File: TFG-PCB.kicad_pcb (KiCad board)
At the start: 2 copper layers, 38.1 x 38.1 mm, 25 parts, among them J1 TYPE-C-31-M-12, SW1 SW_Push, U1 ATmega32U4-AU, Y1 16MHz

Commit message: Added 60% keyboard schematics and started routing wires
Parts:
- added D10: SOD-123, Diode_SMD:D_SOD-123, B.Cu at (304.0, 165.9)
- added D11: SOD-123, Diode_SMD:D_SOD-123, B.Cu at (323.1, 165.9)
- added D12: SOD-123, Diode_SMD:D_SOD-123, B.Cu at (342.1, 165.9)
- added D13: SOD-123, Diode_SMD:D_SOD-123, B.Cu at (361.2, 165.9)
- added D14: SOD-123, Diode_SMD:D_SOD-123, B.Cu at (389.7, 165.9)
- added D15: SOD-123, Diode_SMD:D_SOD-123, B.Cu at (137.3, 184.9)
- added D16: SOD-123, Diode_SMD:D_SOD-123, B.Cu at (161.1, 184.9)
- added D17: SOD-123, Diode_SMD:D_SOD-123, B.Cu at (180.2, 184.9)
- added D18: SOD-123, Diode_SMD:D_SOD-123, B.Cu at (199.2, 184.9)
- added D19: SOD-123, Diode_SMD:D_SOD-123, B.Cu at (218.3, 184.9)
- added D20: SOD-123, Diode_SMD:D_SOD-123, B.Cu at (237.3, 184.9)
- added D21: SOD-123, Diode_SMD:D_SOD-123, B.Cu at (256.4, 184.9)
- added D22: SOD-123, Diode_SMD:D_SOD-123, B.Cu at (275.4, 184.9)
- added D23: SOD-123, Diode_SMD:D_SOD-123, B.Cu at (294.5, 184.9)
- added D24: SOD-123, Diode_SMD:D_SOD-123, B.Cu at (313.5, 184.9)
- added D25: SOD-123, Diode_SMD:D_SOD-123, B.Cu at (332.6, 184.9)
- added D26: SOD-123, Diode_SMD:D_SOD-123, B.Cu at (351.6, 184.9)
- added D27: SOD-123, Diode_SMD:D_SOD-123, B.Cu at (370.7, 184.9)
- added D28: SOD-123, Diode_SMD:D_SOD-123, B.Cu at (396.9, 194.5)
- added D29: SOD-123, Diode_SMD:D_SOD-123, B.Cu at (139.7, 204.0)
- added D30: SOD-123, Diode_SMD:D_SOD-123, B.Cu at (165.9, 204.0)
- added D31: SOD-123, Diode_SMD:D_SOD-123, B.Cu at (184.9, 204.0)
- added D32: SOD-123, Diode_SMD:D_SOD-123, B.Cu at (204.0, 204.0)
- added D33: SOD-123, Diode_SMD:D_SOD-123, B.Cu at (223.0, 204.0)
- added D34: SOD-123, Diode_SMD:D_SOD-123, B.Cu at (242.1, 204.0)
- added D35: SOD-123, Diode_SMD:D_SOD-123, B.Cu at (261.1, 204.0)
- added D36: SOD-123, Diode_SMD:D_SOD-123, B.Cu at (280.2, 204.0)
- added D37: SOD-123, Diode_SMD:D_SOD-123, B.Cu at (299.2, 204.0)
- added D38: SOD-123, Diode_SMD:D_SOD-123, B.Cu at (318.3, 204.0)
- added D39: SOD-123, Diode_SMD:D_SOD-123, B.Cu at (337.3, 204.0)
- added D40: SOD-123, Diode_SMD:D_SOD-123, B.Cu at (356.4, 204.0)
- added D41: SOD-123, Diode_SMD:D_SOD-123, B.Cu at (375.4, 204.0)
- added D42: SOD-123, Diode_SMD:D_SOD-123, B.Cu at (134.9, 223.0)
- added D43: SOD-123, Diode_SMD:D_SOD-123, B.Cu at (156.4, 223.0)
- added D44: SOD-123, Diode_SMD:D_SOD-123, B.Cu at (175.4, 223.0)
- added D45: SOD-123, Diode_SMD:D_SOD-123, B.Cu at (194.5, 223.0)
- added D46: SOD-123, Diode_SMD:D_SOD-123, B.Cu at (213.5, 223.0)
- added D47: SOD-123, Diode_SMD:D_SOD-123, B.Cu at (232.6, 223.0)
- added D48: SOD-123, Diode_SMD:D_SOD-123, B.Cu at (251.6, 223.0)
- added D49: SOD-123, Diode_SMD:D_SOD-123, B.Cu at (270.7, 223.0)
- added D5: SOD-123, Diode_SMD:D_SOD-123, B.Cu at (208.8, 165.9)
- added D50: SOD-123, Diode_SMD:D_SOD-123, B.Cu at (289.7, 223.0)
- added D51: SOD-123, Diode_SMD:D_SOD-123, B.Cu at (308.8, 223.0)
- added D52: SOD-123, Diode_SMD:D_SOD-123, B.Cu at (327.8, 223.0)
- added D53: SOD-123, Diode_SMD:D_SOD-123, B.Cu at (346.9, 223.0)
- added D54: SOD-123, Diode_SMD:D_SOD-123, B.Cu at (382.6, 223.0)
- added D55: SOD-123, Diode_SMD:D_SOD-123, B.Cu at (134.9, 242.1)
- added D56: SOD-123, Diode_SMD:D_SOD-123, B.Cu at (158.8, 242.1)
- added D57: SOD-123, Diode_SMD:D_SOD-123, B.Cu at (182.6, 242.1)
- added D58: SOD-123, Diode_SMD:D_SOD-123, B.Cu at (254.0, 242.1)
- added D59: SOD-123, Diode_SMD:D_SOD-123, B.Cu at (325.4, 242.1)
- added D6: SOD-123, Diode_SMD:D_SOD-123, B.Cu at (227.8, 165.9)
- added D60: SOD-123, Diode_SMD:D_SOD-123, B.Cu at (349.2, 242.1)
- added D61: SOD-123, Diode_SMD:D_SOD-123, B.Cu at (373.1, 242.1)
- added D62: SOD-123, Diode_SMD:D_SOD-123, B.Cu at (396.9, 242.1)
- added D7: SOD-123, Diode_SMD:D_SOD-123, B.Cu at (246.9, 165.9)
- added D8: SOD-123, Diode_SMD:D_SOD-123, B.Cu at (265.9, 165.9)
- added D9: SOD-123, Diode_SMD:D_SOD-123, B.Cu at (285.0, 165.9)
- added MX10: MX-NoLED, MX_Only:MXOnly-1U, F.Cu at (296.1, 164.3)
- added MX11: MX-NoLED, MX_Only:MXOnly-1U, F.Cu at (315.1, 164.3)
- added MX12: MX-NoLED, MX_Only:MXOnly-1U, F.Cu at (334.2, 164.3)
- added MX13: MX-NoLED, MX_Only:MXOnly-1U, F.Cu at (353.2, 164.3)
- added MX14: MX-NoLED, MX_Only:MXOnly-2U, F.Cu at (381.8, 164.3)
- added MX15: MX-NoLED, MX_Only:MXOnly-1.5U, F.Cu at (129.4, 183.4)
- added MX16: MX-NoLED, MX_Only:MXOnly-1U, F.Cu at (153.2, 183.4)
- added MX17: MX-NoLED, MX_Only:MXOnly-1U, F.Cu at (172.2, 183.4)
- added MX18: MX-NoLED, MX_Only:MXOnly-1U, F.Cu at (191.3, 183.4)
- added MX19: MX-NoLED, MX_Only:MXOnly-1U, F.Cu at (210.3, 183.4)
- added MX20: MX-NoLED, MX_Only:MXOnly-1U, F.Cu at (229.4, 183.4)
- added MX21: MX-NoLED, MX_Only:MXOnly-1U, F.Cu at (248.4, 183.4)
- added MX22: MX-NoLED, MX_Only:MXOnly-1U, F.Cu at (267.5, 183.4)
- added MX23: MX-NoLED, MX_Only:MXOnly-1U, F.Cu at (286.5, 183.4)
- added MX24: MX-NoLED, MX_Only:MXOnly-1U, F.Cu at (305.6, 183.4)
- added MX25: MX-NoLED, MX_Only:MXOnly-1U, F.Cu at (324.6, 183.4)
- added MX26: MX-NoLED, MX_Only:MXOnly-1U, F.Cu at (343.7, 183.4)
- added MX27: MX-NoLED, MX_Only:MXOnly-1U, F.Cu at (362.7, 183.4)
- added MX28: MX-NoLED, MX_Only:MXOnly-ISO, F.Cu at (388.9, 192.9)
- added MX29: MX-NoLED, MX_Only:MXOnly-1.75U, F.Cu at (131.8, 202.4)
- added MX30: MX-NoLED, MX_Only:MXOnly-1U, F.Cu at (158.0, 202.4)
- added MX31: MX-NoLED, MX_Only:MXOnly-1U, F.Cu at (177.0, 202.4)
- added MX32: MX-NoLED, MX_Only:MXOnly-1U, F.Cu at (196.1, 202.4)
- added MX33: MX-NoLED, MX_Only:MXOnly-1U, F.Cu at (215.1, 202.4)
- added MX34: MX-NoLED, MX_Only:MXOnly-1U, F.Cu at (234.2, 202.4)
- added MX35: MX-NoLED, MX_Only:MXOnly-1U, F.Cu at (253.2, 202.4)
- added MX36: MX-NoLED, MX_Only:MXOnly-1U, F.Cu at (272.3, 202.4)
- added MX37: MX-NoLED, MX_Only:MXOnly-1U, F.Cu at (291.3, 202.4)
- added MX38: MX-NoLED, MX_Only:MXOnly-1U, F.Cu at (310.4, 202.4)
- added MX39: MX-NoLED, MX_Only:MXOnly-1U, F.Cu at (329.4, 202.4)
- added MX40: MX-NoLED, MX_Only:MXOnly-1U, F.Cu at (348.5, 202.4)
- added MX41: MX-NoLED, MX_Only:MXOnly-1U, F.Cu at (367.5, 202.4)
- added MX42: MX-NoLED, MX_Only:MXOnly-1.25U, F.Cu at (127.0, 221.5)
- added MX43: MX-NoLED, MX_Only:MXOnly-1U, F.Cu at (148.4, 221.5)
- added MX44: MX-NoLED, MX_Only:MXOnly-1U, F.Cu at (167.5, 221.5)
- added MX45: MX-NoLED, MX_Only:MXOnly-1U, F.Cu at (186.5, 221.5)
- added MX46: MX-NoLED, MX_Only:MXOnly-1U, F.Cu at (205.6, 221.5)
- added MX47: MX-NoLED, MX_Only:MXOnly-1U, F.Cu at (224.6, 221.5)
- added MX48: MX-NoLED, MX_Only:MXOnly-1U, F.Cu at (243.7, 221.5)
- added MX49: MX-NoLED, MX_Only:MXOnly-1U, F.Cu at (262.7, 221.5)
- added MX5: MX-NoLED, MX_Only:MXOnly-1U, F.Cu at (200.8, 164.3)
- added MX50: MX-NoLED, MX_Only:MXOnly-1U, F.Cu at (281.8, 221.5)
- added MX51: MX-NoLED, MX_Only:MXOnly-1U, F.Cu at (300.8, 221.5)
- added MX52: MX-NoLED, MX_Only:MXOnly-1U, F.Cu at (319.9, 221.5)
- added MX53: MX-NoLED, MX_Only:MXOnly-1U, F.Cu at (338.9, 221.5)
- added MX54: MX-NoLED, MX_Only:MXOnly-2.75U, F.Cu at (374.6, 221.5)
- added MX55: MX-NoLED, MX_Only:MXOnly-1.25U, F.Cu at (127.0, 240.5)
- added MX56: MX-NoLED, MX_Only:MXOnly-1.25U, F.Cu at (150.8, 240.5)
- added MX57: MX-NoLED, MX_Only:MXOnly-1.25U, F.Cu at (174.6, 240.5)
- added MX58: MX-NoLED, MX_Only:MXOnly-6.25U, F.Cu at (246.1, 240.5)
- added MX59: MX-NoLED, MX_Only:MXOnly-1.25U, F.Cu at (317.5, 240.5)
- added MX6: MX-NoLED, MX_Only:MXOnly-1U, F.Cu at (219.9, 164.3)
- added MX60: MX-NoLED, MX_Only:MXOnly-1.25U, F.Cu at (341.3, 240.5)
- added MX61: MX-NoLED, MX_Only:MXOnly-1.25U, F.Cu at (365.1, 240.5)
- added MX62: MX-NoLED, MX_Only:MXOnly-1.25U, F.Cu at (388.9, 240.5)
- added MX7: MX-NoLED, MX_Only:MXOnly-1U, F.Cu at (238.9, 164.3)
- added MX8: MX-NoLED, MX_Only:MXOnly-1U, F.Cu at (258.0, 164.3)
- added MX9: MX-NoLED, MX_Only:MXOnly-1U, F.Cu at (277.0, 164.3)
- C1, C2: value 0.1uF -> 22pF
- C3: value 0.1uF -> 1uF
- C4, C5: value 22pF -> 0.1uF
- C6: value 10uF -> 0.1uF
- C7: value 1uF -> 10uF
- R1: value 22 -> 10k
- R3: value 10k -> 22
- R4: value 10k -> 5.1k
- R5: value 5.1k -> 10k; moved to B.Cu
- SW1: moved to B.Cu
- moved SW1 234.1 mm to (225.4, 246.1), turned to 180 degrees
- moved R5 209.1 mm to (219.9, 227.0), turned to 180 degrees
- moved R1 191.1 mm to (207.2, 248.4), turned to 180 degrees
- moved C7 182.7 mm to (215.7, 246.8), turned to 270 degrees
- moved C1 180.1 mm to (207.2, 245.7), turned to 180 degrees
- moved C6 175.4 mm to (226.2, 239.6), turned to 90 degrees
- moved C4 172.7 mm to (204.2, 240.7), turned to 0 degrees
- moved U1 168.5 mm to (215.7, 236.6), turned to 90 degrees
- moved Y1 166.8 mm to (204.1, 236.5), turned to 270 degrees
- moved C3 166.3 mm to (226.1, 233.0), turned to 270 degrees
- moved C5 161.0 mm to (204.2, 232.4), turned to 180 degrees
- moved C2 154.6 mm to (212.8, 227.1), turned to 180 degrees
- moved R4 111.7 mm to (156.4, 148.4)
- moved F1 104.9 mm to (156.4, 143.7)
- moved J1 104.5 mm to (134.1, 154.0)
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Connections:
- C1 pad 1: +5V -> Net-(C1-Pad1)
- C2 pad 1: +5V -> Net-(C2-Pad1)
- C3 pad 1: +5V -> Net-(C3-Pad1)
- C4 pad 1: Net-(C4-Pad1) -> +5V
- C5 pad 1: Net-(C5-Pad1) -> +5V
- C7 pad 1: Net-(C7-Pad1) -> +5V
- D2 pad 1: ROW1 -> ROW0
- D4 pad 1: ROW1 -> ROW0
- MX2 pad 1: COL0 -> COL1
- MX3 pad 1: COL1 -> COL2
- MX4 pad 1: COL1 -> COL3
- R1 pad 1: Net-(R1-Pad1) -> +5V
- R1 pad 2: D- -> Net-(R1-Pad2)
- R3 pad 1: +5V -> Net-(R3-Pad1)
- R3 pad 2: Net-(R3-Pad2) -> D-
- R4 pad 2: Net-(R4-Pad2) -> Net-(J1-PadB5)
- R5 pad 2: Net-(J1-PadB5) -> Net-(R5-Pad2)
- SW1 pad 2: Net-(R3-Pad2) -> Net-(R1-Pad2)
- U1 pad 13: Net-(R3-Pad2) -> Net-(R1-Pad2)
- U1 pad 16: Net-(C5-Pad1) -> Net-(C2-Pad1)
- U1 pad 17: Net-(C4-Pad1) -> Net-(C1-Pad1)
- U1 pad 3: Net-(R1-Pad1) -> Net-(R3-Pad1)
- U1 pad 33: Net-(R4-Pad2) -> Net-(R5-Pad2)
- U1 pad 6: Net-(C7-Pad1) -> Net-(C3-Pad1)
- Y1 pad 1: Net-(C4-Pad1) -> Net-(C1-Pad1)
- Y1 pad 3: Net-(C5-Pad1) -> Net-(C2-Pad1)
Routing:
- net ROW1: track 0.00 -> 263.5 mm
- net ROW0: track 0.00 -> 257.2 mm
- net ROW3: track 0.00 -> 247.6 mm
- net ROW2: track 0.00 -> 235.7 mm
- net ROW4: track 0.00 -> 190.5 mm
- net COL1: track 0.00 -> 87.6 mm
- net COL0: track 0.00 -> 82.2 mm
- net COL4: track 0.00 -> 23.0 mm
- net COL5: track 0.00 -> 23.0 mm
- net COL2: track 0.00 -> 23.0 mm
- net COL3: track 0.00 -> 23.0 mm
- net Net-(D9-Pad2): track 0.00 -> 7.90 mm
- net Net-(D52-Pad2): track 0.00 -> 7.90 mm
- net Net-(D51-Pad2): track 0.00 -> 7.90 mm
- net Net-(D10-Pad2): track 0.00 -> 7.90 mm
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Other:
- board outline removed
- net class Default: trace_width 0.25 -> 0.254
- net class Power added: clearance 0.2, trace_width 0.381, via_dia 0.8, via_drill 0.4

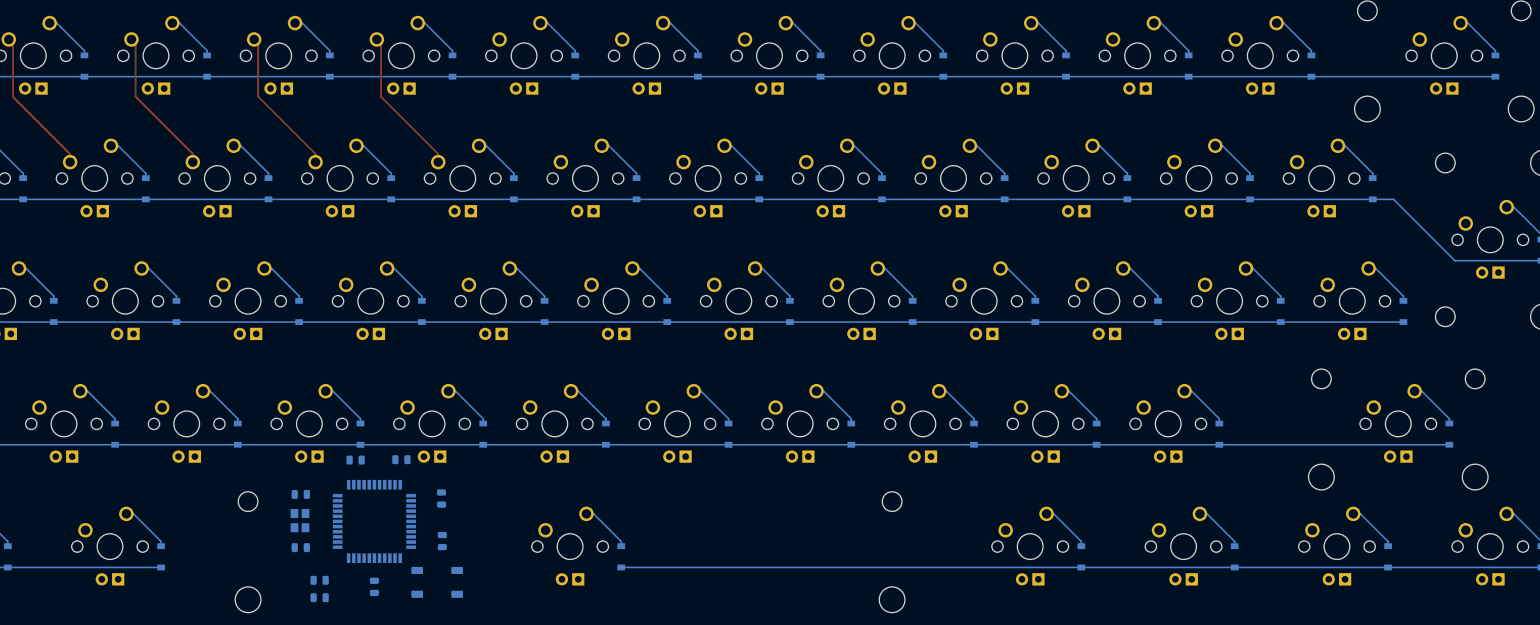
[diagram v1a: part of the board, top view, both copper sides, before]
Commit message: Renamed Footprints to account for keys
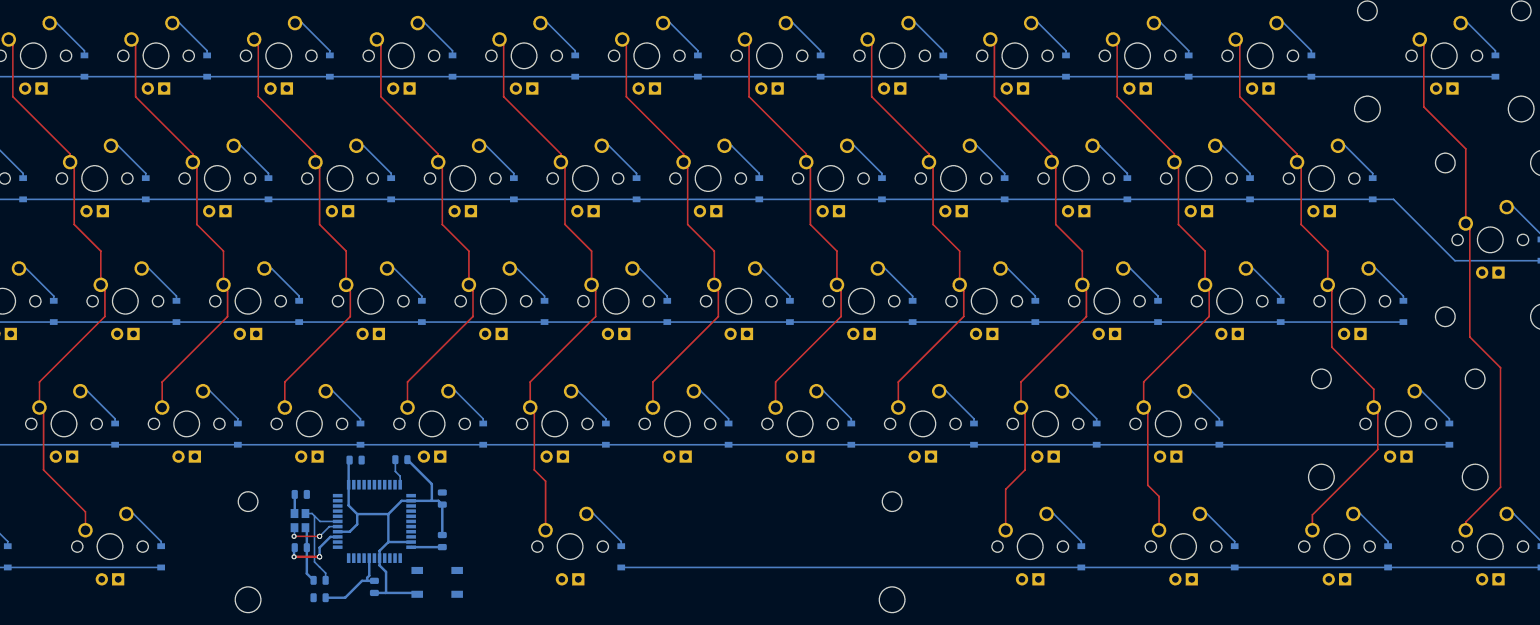
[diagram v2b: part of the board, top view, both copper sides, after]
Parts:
- moved C3 0.13 mm to (226.2, 233.0)
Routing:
- net COL12: track 0.00 -> 89.5 mm
- net COL10: track 0.00 -> 88.1 mm
- net COL11: track 0.00 -> 87.6 mm
- net COL6: track 0.00 -> 87.6 mm
- net COL13: track 0.00 -> 83.6 mm
- net GND: track 0.00 -> 76.3 mm
- net COL7: track 0.00 -> 67.5 mm
- net COL8: track 0.00 -> 67.5 mm
- net COL9: track 0.00 -> 67.5 mm
- net COL2: track 23.0 -> 89.5 mm
- net COL3: track 23.0 -> 67.5 mm
- net COL4: track 23.0 -> 67.5 mm
- net COL5: track 23.0 -> 67.5 mm
- net +5V: track 0.00 -> 27.5 mm, vias 0 -> 3
- net Net-(C1-Pad1): track 0.00 -> 16.2 mm
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
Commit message: Edge cuts + wiring removal
Removed all wires, slightly adjusted diode positions so they fit outside the switch courtyards + created the edge cuts that represent the board edges
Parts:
- MX1: value MX-NoLED -> Esc
- MX10: value MX-NoLED -> 9
- MX11: value MX-NoLED -> 0
- MX12: value MX-NoLED -> -
- MX13: value MX-NoLED -> =
- MX14: value MX-NoLED -> BkSpc
- MX15: value MX-NoLED -> Tab
- MX16: value MX-NoLED -> Q
- MX17: value MX-NoLED -> W
- MX18: value MX-NoLED -> E
- MX19: value MX-NoLED -> R
- MX2: value MX-NoLED -> 1
- MX20: value MX-NoLED -> T
- MX21: value MX-NoLED -> Y
- MX22: value MX-NoLED -> U
- MX23: value MX-NoLED -> I
- MX24: value MX-NoLED -> O
- MX25: value MX-NoLED -> P
- MX26: value MX-NoLED -> [
- MX27: value MX-NoLED -> ]
- MX28: value MX-NoLED -> Enter
- MX29: value MX-NoLED -> CapsLck
- MX3: value MX-NoLED -> 2
- MX30: value MX-NoLED -> A
- MX31: value MX-NoLED -> S
- MX32: value MX-NoLED -> D
- MX33: value MX-NoLED -> F
- MX34: value MX-NoLED -> G
- MX35: value MX-NoLED -> H
- MX36: value MX-NoLED -> J
- MX37: value MX-NoLED -> K
- MX38: value MX-NoLED -> L
- MX39: value MX-NoLED -> ;
- MX4: value MX-NoLED -> 3
- MX40: value MX-NoLED -> '
- MX41: value MX-NoLED -> #
- MX42: value MX-NoLED -> LShift
- MX43: value MX-NoLED -> \
- MX44: value MX-NoLED -> Z
- MX45: value MX-NoLED -> X
- MX46: value MX-NoLED -> C
- MX47: value MX-NoLED -> V
- MX48: value MX-NoLED -> B
- MX49: value MX-NoLED -> N
- MX5: value MX-NoLED -> 4
- MX50: value MX-NoLED -> M
- MX51: value MX-NoLED -> ,
- MX52: value MX-NoLED -> .
- MX53: value MX-NoLED -> /
- MX54: value MX-NoLED -> RShift
- MX55: value MX-NoLED -> LCtrl
- MX56: value MX-NoLED -> LWin
- MX57: value MX-NoLED -> LAlt
- MX58: value MX-NoLED -> Space
- MX59: value MX-NoLED -> RAlt
- MX6: value MX-NoLED -> 5
- MX60: value MX-NoLED -> RWin
- MX61: value MX-NoLED -> RCtrl
- MX62: value MX-NoLED -> Fn
- MX7: value MX-NoLED -> 6
- MX8: value MX-NoLED -> 7
- MX9: value MX-NoLED -> 8
- moved D11 0.79 mm to (323.9, 165.9)
- moved D22 0.79 mm to (276.2, 184.9)
- moved D27 0.79 mm to (371.5, 184.9)
- moved D37 0.79 mm to (300.0, 204.0)
- moved D53 0.79 mm to (347.7, 223.0)
- moved D54 0.79 mm to (383.4, 223.0)
- moved D15 0.79 mm to (138.1, 184.9)
- moved D16 0.79 mm to (161.9, 184.9)
- moved D18 0.79 mm to (200.0, 184.9)
- moved D2 0.79 mm to (152.4, 165.9)
- moved D29 0.79 mm to (140.5, 204.0)
- moved D31 0.79 mm to (185.7, 204.0)
- moved D33 0.79 mm to (223.8, 204.0)
- moved D44 0.79 mm to (176.2, 223.0)
- moved D47 0.79 mm to (233.4, 223.0)
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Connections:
- J1 pad A5: Net-(J1-PadA5) -> CC1
- J1 pad B5: Net-(J1-PadB5) -> CC1
- R4 pad 2: Net-(J1-PadB5) -> CC1
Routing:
- net ROW1: track 263.5 -> 0.00 mm
- net ROW0: track 257.2 -> 0.00 mm
- net ROW3: track 247.6 -> 0.00 mm
- net ROW2: track 235.7 -> 0.00 mm
- net ROW4: track 190.5 -> 0.00 mm
- net COL2: track 89.5 -> 0.00 mm
- net COL12: track 89.5 -> 0.00 mm
- net COL10: track 88.1 -> 0.00 mm
- net COL11: track 87.6 -> 0.00 mm
- net COL6: track 87.6 -> 0.00 mm
- net COL1: track 87.6 -> 0.00 mm
- net COL13: track 83.6 -> 0.00 mm
- net COL0: track 82.2 -> 0.00 mm
- net GND: track 76.3 -> 0.00 mm
- net COL7: track 67.5 -> 0.00 mm
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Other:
- board outline added: 287.3 x 99.2 mm

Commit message: Moved diodes + started wiring
Moved diodes (again) and started differential wiring
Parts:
- moved C4 76.9 mm to (275.4, 269.9), turned to 180 degrees
- moved C5 75.6 mm to (269.9, 269.9), turned to 0 degrees
- moved R5 62.8 mm to (253.2, 280.2), turned to 0 degrees
- moved R1 58.9 mm to (265.1, 258.8), turned to 0 degrees
- moved C3 45.7 mm to (246.1, 274.2), turned to 90 degrees
- moved C7 43.2 mm to (256.6, 260.4), turned to 90 degrees
- moved C6 34.2 mm to (246.1, 267.6), turned to 270 degrees
- moved SW1 26.2 mm to (246.9, 261.1), turned to 0 degrees
- moved Y1 21.7 mm to (225.4, 240.6), turned to 90 degrees
- moved C1 15.3 mm to (222.2, 242.9), turned to 270 degrees
- moved C2 15.2 mm to (222.2, 238.9), turned to 270 degrees
- moved R2 14.8 mm to (135.7, 162.7)
- moved R3 14.8 mm to (132.6, 162.7)
- moved U1 5.21 mm to (212.2, 240.4), turned to 270 degrees
- moved D15 3.18 mm to (138.1, 188.1)
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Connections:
- net Net-(R2-Pad1) renamed /D_P
- net Net-(R3-Pad1) renamed /D_N
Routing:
- net /D_N: track 0.00 -> 139.9 mm
- net /D_P: track 0.00 -> 138.8 mm
- net Net-(C2-Pad1): track 0.00 -> 10.0 mm
- net Net-(C1-Pad1): track 0.00 -> 7.46 mm
- net D+: track 0.00 -> 6.06 mm
- net D-: track 0.00 -> 4.48 mm
